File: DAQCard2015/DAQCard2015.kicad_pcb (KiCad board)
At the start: 4 copper layers, 160 x 160 mm, 215 parts, among them CON1 BARREL_JACK, K1 1462042-8, P1 QTH-090-01-F-D-A, P10 GND, P11 70246-1004, P2 QTH-090-01-F-D-A, P3 miniDIL20, P4 LEMO_EPY.00.250.NTN, P5 LEMO_EPY.00.250.NTN, P6 FAN, P7 CONN_02X20_Double, P8 GND, P9 SHV, Q1 MMBT2222A-TP, Q2 SBC817-40LT1G, SW1 DPDT, U1 RJ45x8, U10 AD9219, U11 THS4524IDBTR, U12 AD9219, U13 THS4524IDBTR, U14 AD9219, U15 THS4524IDBTR, U16 AD9219, U17 THS4524IDBTR, U18 AD9219, U19 AD8534, U2 AD5628, U20 LM1086_1V8, U21 LT1913, U22 AD5628, U23 AD8534, U24 MCP65R41, U25 LM1086_2V5, U26 TLC59282, U3 THS4524IDBTR, U4 AD9219, U5 THS4524IDBTR, U6 AD9219, U7 THS4524IDBTR, U8 AD9219, U9 THS4524IDBTR

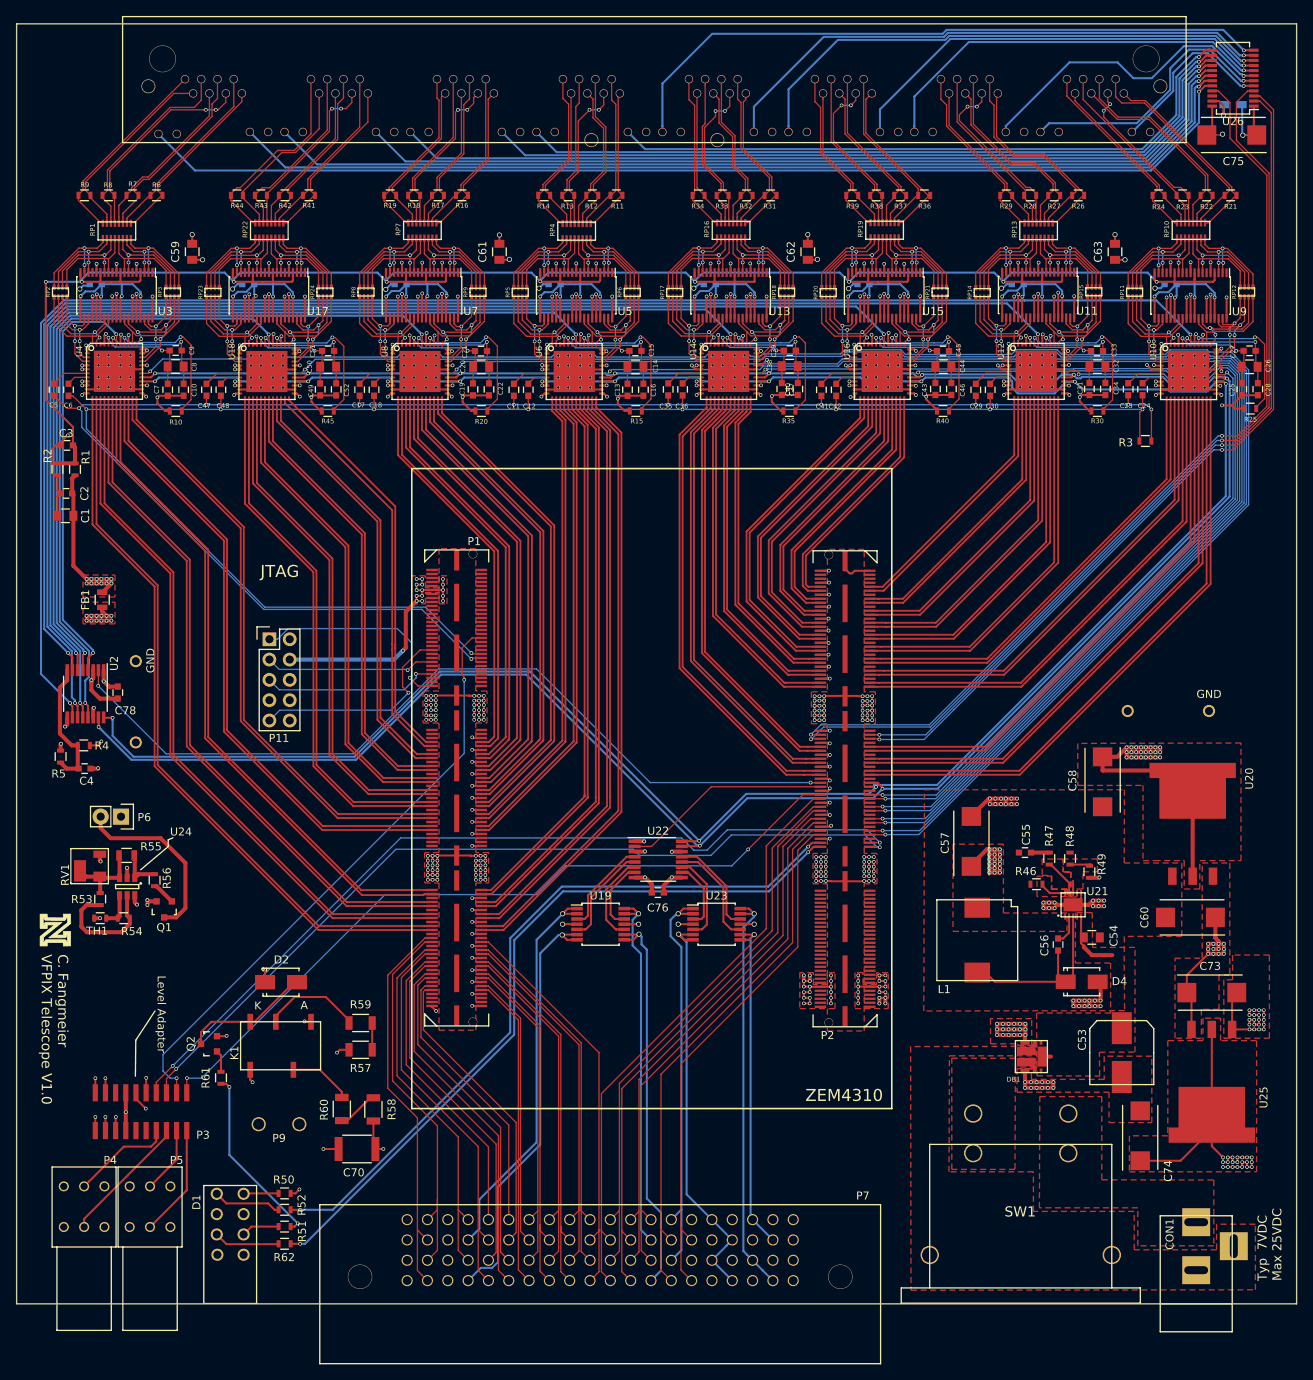
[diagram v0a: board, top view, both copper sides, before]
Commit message: Adds digipart field to all parts that is now used in automatic generation of BOM(see DAQCard2015.html)
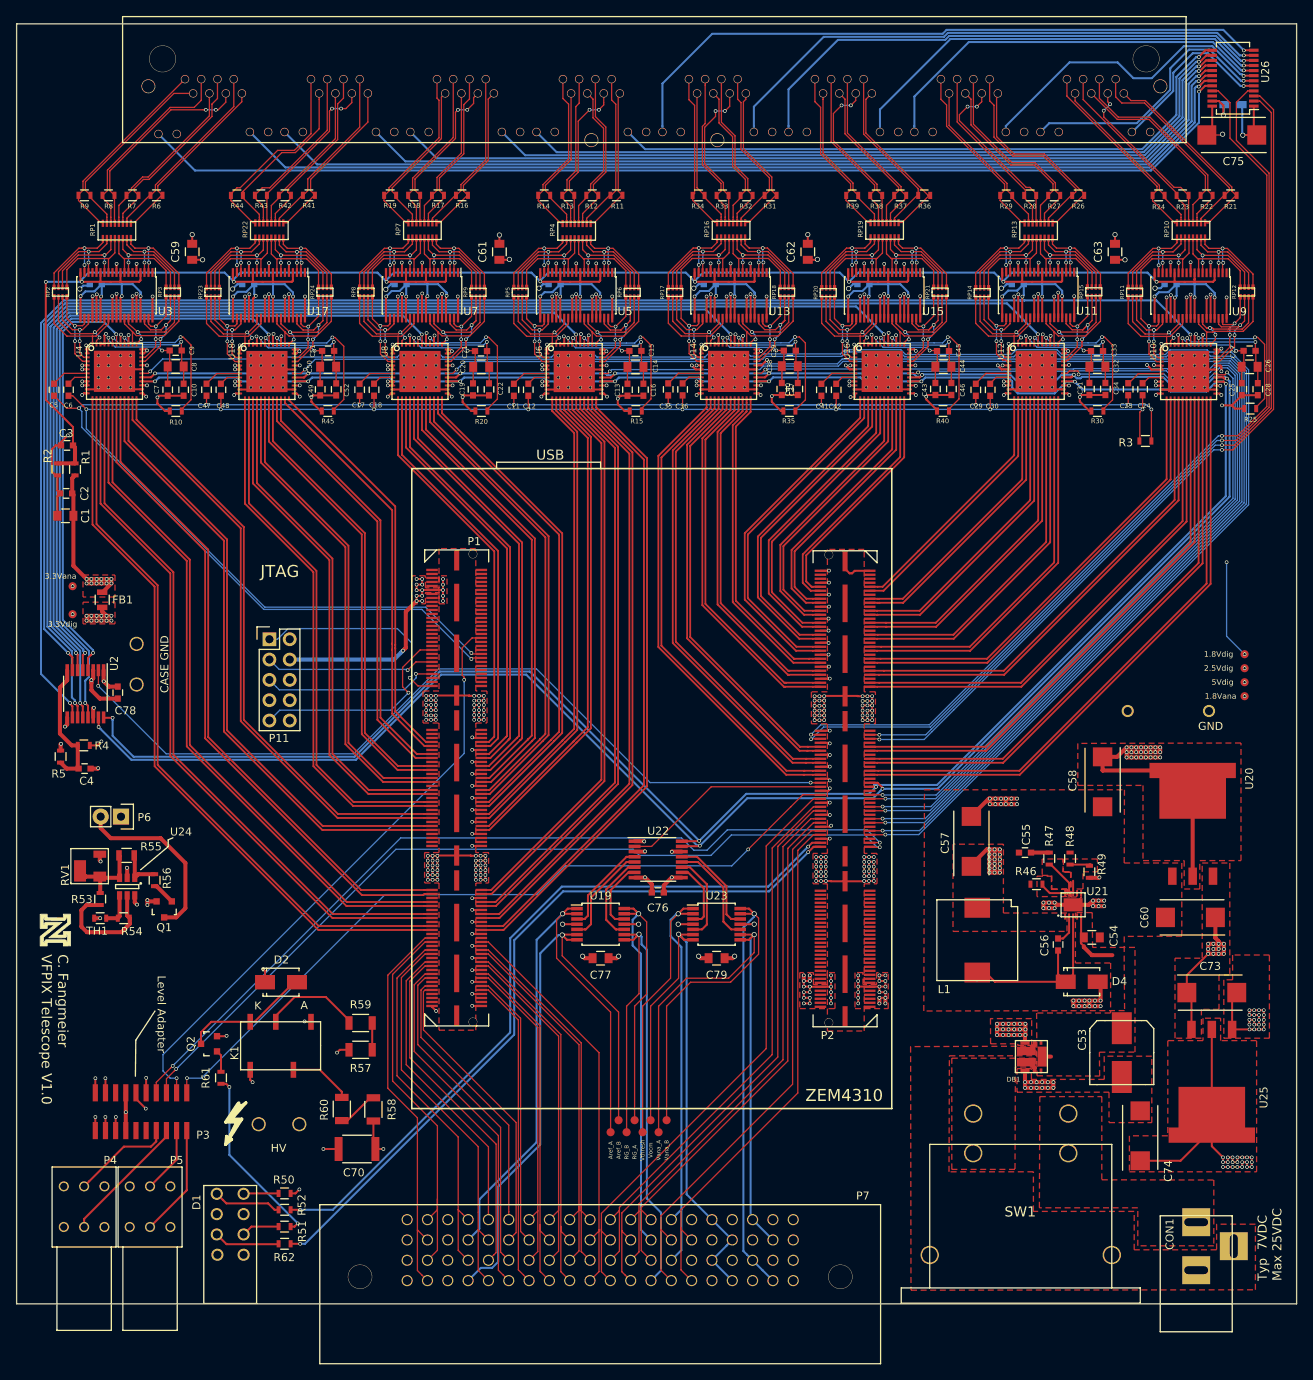
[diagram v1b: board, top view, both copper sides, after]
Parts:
- removed P10: GND, extras:Harwin_D3082-05
- added C77: 10uF, Capacitors_SMD:C_0805, F.Cu at (91.0, 141.0)
- added C79: 10uF, Capacitors_SMD:C_0805, F.Cu at (105.5, 141.0)
- added P12: 5Vdig, extras:testpad, F.Cu at (171.5, 106.5)
- added P13: 1.8Vana, extras:testpad, F.Cu at (171.5, 108.2)
- added P14: 1.8Vdig, extras:testpad, F.Cu at (171.5, 103.0)
- added P15: 3.3Vdig, extras:testpad, F.Cu at (25.0, 98.0)
- added P16: 3.3Vana, extras:testpad, F.Cu at (25.0, 94.5)
- added P17: 2.5Vdig, extras:testpad, F.Cu at (171.5, 104.8)
- added P18: Aref_A, extras:testpad, F.Cu at (92.2, 162.8)
- added P19: Aref_B, extras:testpad, F.Cu at (93.2, 161.2)
- added P20: RG_A, extras:testpad, F.Cu at (95.2, 161.2)
- added P21: RG_B, extras:testpad, F.Cu at (94.2, 162.8)
- added P22: Vthresh, extras:testpad, F.Cu at (96.2, 162.8)
- added P23: Vocm, extras:testpad, F.Cu at (97.2, 161.2)
- added P24: Vana_B, extras:testpad, F.Cu at (99.2, 161.2)
- added P25: Vana_A, extras:testpad, F.Cu at (98.2, 162.8)
- added P26: CASE GND, extras:TE_1217133-1, F.Cu at (33.0, 104.2)
- added REF**: Symbol_Highvoltage_Type1_CopperTop_Small, extras:Symbol_Highvoltage_Type1_CopperTop_Small, F.Cu at (44.5, 162.2)
- C58, C74: value 100uF -> 10uF
- P9: value SHV -> HV
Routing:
- net 2V5dig: track 117.2 -> 181.5 mm, vias 21 -> 22
- net 5Vdig: track 77.2 -> 115.9 mm, vias 73 -> 76
- net Vana_B: track 51.7 -> 85.4 mm
- net 1V8dig: track 45.8 -> 79.4 mm, vias 32 -> 34
- net Vana_A: track 43.3 -> 76.0 mm
- net Aref_A: track 49.5 -> 79.9 mm
- net Vthresh: track 50.7 -> 79.8 mm
- net RG_A: track 45.9 -> 72.7 mm
- net Aref_B: track 53.1 -> 79.2 mm
- net RG_B: track 49.0 -> 74.4 mm
- net Vocm_tel: track 52.1 -> 76.8 mm
- net 1V8ana: track 141.5 -> 156.6 mm, vias 112 -> 113
- net GND: track 541.3 -> 544.1 mm, vias 357 -> 359
- net /Frontend/4DCO-: track 76.0 -> 78.6 mm
- net /Frontend/4DCO+: track 76.6 -> 79.2 mm
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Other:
- board text added: "USB"

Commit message: Final Pre-order updates for DAQCard2015
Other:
- board text added: "+/-"
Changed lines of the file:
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@@
-(kicad_pcb (version 4) (host pcbnew "(2015-09-23 BZR 6209)-product")
+(kicad_pcb (version 4) (host pcbnew "(2015-10-06 BZR 6248)-product")
   (general
     (links 1466)
@@
     (area 17.924999 24.124999 178.075001 184.275001)
     (thickness 1.6)
-    (drawings 28)
+    (drawings 37)
     (tracks 6714)
     (zones 0)
@@
   )
   (setup
-    (last_trace_width 0.508)
+    (last_trace_width 0.1524)
     (user_trace_width 0.1524)
     (user_trace_width 0.254)
@@
     (tags "capacitor 0603")
     (attr smd)
-    (fp_text reference C64 (at 0 1.9) (layer B.SilkS)
+    (fp_text reference C64 (at 3.1 -0.05) (layer B.SilkS)
       (effects (font (size 1 1) (thickness 0.15)) (justify mirror))
     )
@@
     (tags "capacitor 0603")
     (attr smd)
-    (fp_text reference C65 (at 0 1.9) (layer B.SilkS)
+    (fp_text reference C65 (at 3.15 -0.05) (layer B.SilkS)
       (effects (font (size 1 1) (thickness 0.15)) (justify mirror))
     )
@@
     (tags "capacitor 0603")
     (attr smd)
-    (fp_text reference C66 (at 0 1.9) (layer B.SilkS)
+    (fp_text reference C66 (at 3 -0.05) (layer B.SilkS)
       (effects (font (size 1 1) (thickness 0.15)) (justify mirror))
     )
@@
     (tags "capacitor 0603")
     (attr smd)
-    (fp_text reference C67 (at 0 1.9) (layer B.SilkS)
+    (fp_text reference C67 (at 2.95 0.05) (layer B.SilkS)
       (effects (font (size 1 1) (thickness 0.15)) (justify mirror))
     )
@@
     (tags "capacitor 0603")
     (attr smd)
-    (fp_text reference C68 (at 0 1.9) (layer B.SilkS)
+    (fp_text reference C68 (at 2.85 0.05) (layer B.SilkS)
       (effects (font (size 1 1) (thickness 0.15)) (justify mirror))
     )
@@
     (tags "capacitor 0603")
     (attr smd)
-    (fp_text reference C69 (at 0 1.9) (layer B.SilkS)
+    (fp_text reference C69 (at 3.05 -0.05) (layer B.SilkS)
       (effects (font (size 1 1) (thickness 0.15)) (justify mirror))
     )
@@
     (tags "capacitor 0603")
     (attr smd)
-    (fp_text reference C71 (at 0 1.9) (layer B.SilkS)
+    (fp_text reference C71 (at 2.95 0.05) (layer B.SilkS)
       (effects (font (size 1 1) (thickness 0.15)) (justify mirror))
     )
@@
     (tags "capacitor 0603")
     (attr smd)
-    (fp_text reference C72 (at 0 1.9) (layer B.SilkS)
+    (fp_text reference C72 (at 2.95 0.05) (layer B.SilkS)
       (effects (font (size 1 1) (thickness 0.15)) (justify mirror))
     )
@@
     )
   )
+  (gr_line (start 173.825823 178.167807) (end 173.825823 179.467807) (layer F.SilkS) (width 0.1778))
+  (gr_line (start 173.825823 176.967807) (end 173.825823 175.267807) (layer F.SilkS) (width 0.1778))
+  (gr_arc (start 173.825823 177.867807) (end 172.925823 177.867807) (angle 180) (layer F.SilkS) (width 0.1778))
+  (gr_circle (center 173.825823 177.867807) (end 173.725823 177.767807) (layer F.SilkS) (width 0.508))
+  (gr_text +/- (at 173.825823 174.467807 180) (layer F.SilkS)
+    (effects (font (size 0.762 0.762) (thickness 0.1905)))
+  )
+  (gr_text +/- (at 173.925823 180.267807 360) (layer F.SilkS)
+    (effects (font (size 0.762 0.762) (thickness 0.1905)))
+  )
+  (dimension 160 (width 0.3) (layer Cmts.User)
+    (gr_text "6.2992 in" (at 7.25 104.2 90) (layer Cmts.User)
+      (effects (font (size 1.5 1.5) (thickness 0.3)))
+    )
+    (feature1 (pts (xy 18 24.2) (xy 5.9 24.2)))
+    (feature2 (pts (xy 18 184.2) (xy 5.9 184.2)))
+    (crossbar (pts (xy 8.6 184.2) (xy 8.6 24.2)))
+    (arrow1a (pts (xy 8.6 24.2) (xy 9.186421 25.326504)))
+    (arrow1b (pts (xy 8.6 24.2) (xy 8.013579 25.326504)))
+    (arrow2a (pts (xy 8.6 184.2) (xy 9.186421 183.073496)))
+    (arrow2b (pts (xy 8.6 184.2) (xy 8.013579 183.073496)))
+  )
+  (dimension 160 (width 0.3) (layer Cmts.User)
+    (gr_text "6.2992 in" (at 98 189.949999) (layer Cmts.User)
+      (effects (font (size 1.5 1.5) (thickness 0.3)))
+    )
+    (feature1 (pts (xy 178 184.2) (xy 178 191.299999)))
+    (feature2 (pts (xy 18 184.2) (xy 18 191.299999)))
+    (crossbar (pts (xy 18 188.599999) (xy 178 188.599999)))
+    (arrow1a (pts (xy 178 188.599999) (xy 176.873496 189.18642)))
+    (arrow1b (pts (xy 178 188.599999) (xy 176.873496 188.013578)))
+    (arrow2a (pts (xy 18 188.599999) (xy 19.126504 189.18642)))
+    (arrow2b (pts (xy 18 188.599999) (xy 19.126504 188.013578)))
+  )
+  (gr_line (start 76.7 90) (end 125.8 90) (layer Cmts.User) (width 0.02))
   (gr_line (start 91 79) (end 91 79.8) (layer F.SilkS) (width 0.07))
   (gr_line (start 78 79) (end 91 79) (layer F.SilkS) (width 0.07))
@@
     (effects (font (size 1.016 1.016) (thickness 0.1778)))
   )
-  (gr_text "Typ  7VDC\nMax 25VDC" (at 174.65 181.35 90) (layer F.SilkS)
+  (gr_text "Typ  7VDC\nMax 25VDC" (at 165.9 170 360) (layer F.SilkS)
     (effects (font (size 1.143 1.143) (thickness 0.2032)) (justify left))
   )
@@
   (segment (start 106.761501 176.918499) (end 104.92 178.76) (width 0.254) (layer B.Cu) (net 435))
   (segment (start 107.46 176.22) (end 104.92 173.68) (width 0.254) (layer B.Cu) (net 435))
+  (segment (start 172.4 165.9) (end 174.331801 163.968199) (width 0.1524) (layer B.Cu) (net 436))
+  (segment (start 174.331801 163.968199) (end 174.331801 105.831801) (width 0.1524) (layer B.Cu) (net 436))
+  (segment (start 174.331801 105.831801) (end 173.25 104.75) (width 0.1524) (layer B.Cu) (net 436))
+  (segment (start 173.25 104.75) (end 171.5 104.75) (width 0.1524) (layer B.Cu) (net 436))
   (via (at 171.5 104.75) (size 0.4572) (drill 0.3048) (layers F.Cu B.Cu) (net 436))
   (segment (start 172.4 165.9) (end 172.723289 165.9) (width 0.1524) (layer POWER.Cu) (net 436))
-  (segment (start 172.723289 165.9) (end 174.331801 164.291488) (width 0.1524) (layer POWER.Cu) (net 436))
-  (segment (start 173.25 104.75) (end 171.5 104.75) (width 0.1524) (layer POWER.Cu) (net 436))
-  (segment (start 174.331801 164.291488) (end 174.331801 105.831801) (width 0.1524) (layer POWER.Cu) (net 436))
-  (segment (start 174.331801 105.831801) (end 173.25 104.75) (width 0.1524) (layer POWER.Cu) (net 436))
   (segment (start 110 181.3) (end 111.206499 180.093501) (width 0.254) (layer POWER.Cu) (net 436))
   (segment (start 121.87784 170.02216) (end 123.178384 168.721616) (width 0.254) (layer POWER.Cu) (net 436))
@@
     (polygon
       (pts
-        (xy 25.6 70) (xy 25.6 62) (xy 175.1 61.8) (xy 175.1 116.65) (xy 155.85 116.65)
+        (xy 25.6 70) (xy 25.6 62) (xy 177 61.9) (xy 177 116.6) (xy 155.85 116.65)
         (xy 155.85 112.9) (xy 162.55 112.9) (xy 162.5 91.5) (xy 169.25 91.45) (xy 169.25 70)
       )
@@
     (polygon
       (pts
-        (xy 178 184.2) (xy 178 24.2) (xy 18 24.2) (xy 18 184.2)
+        (xy 177 183.2) (xy 177 25.2) (xy 19 25.2) (xy 19 183.2)
       )
     )
@@
       (pts
         (xy 23.075 96.017236) (xy 31.9 96.15) (xy 31.915554 88.95) (xy 31.85 73.4) (xy 25.6 73.4)
-        (xy 25.594796 61.990791) (xy 177.75 61.8) (xy 177.75 51.25) (xy 23.175 51.1)
+        (xy 25.594796 61.990791) (xy 177 61.8) (xy 177 51.2) (xy 23.175 51.1)
       )
     )
@@
         (xy 120.5 91.5) (xy 116.5 91.5) (xy 116.5 125) (xy 80.2 125) (xy 80.2 112)
         (xy 74 112) (xy 37.5 112) (xy 37.5 96.5) (xy 23.00473 96.5) (xy 23 51)
-        (xy 177 51) (xy 177 24.75) (xy 18.5 24.75) (xy 18.5 96.5) (xy 18.5 138.5)
-        (xy 31 138.5) (xy 31 164) (xy 32.5 164) (xy 32.5 138.5) (xy 39.079783 138.5)
-        (xy 39 126) (xy 29.5 126) (xy 29.5 120.5) (xy 48 120.5) (xy 47.919331 138.5)
-        (xy 74 138.5)
+        (xy 177 51) (xy 177 25.2) (xy 19 25.2) (xy 19 138.5) (xy 31 138.5)
+        (xy 31 164) (xy 32.5 164) (xy 32.5 138.5) (xy 39.079783 138.5) (xy 39 126)
+        (xy 29.5 126) (xy 29.5 120.5) (xy 48 120.5) (xy 47.919331 138.5) (xy 74 138.5)
       )
     )
